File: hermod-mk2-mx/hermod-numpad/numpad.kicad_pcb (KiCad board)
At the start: 2 copper layers, 92.1 x 99.3 mm, 48 parts

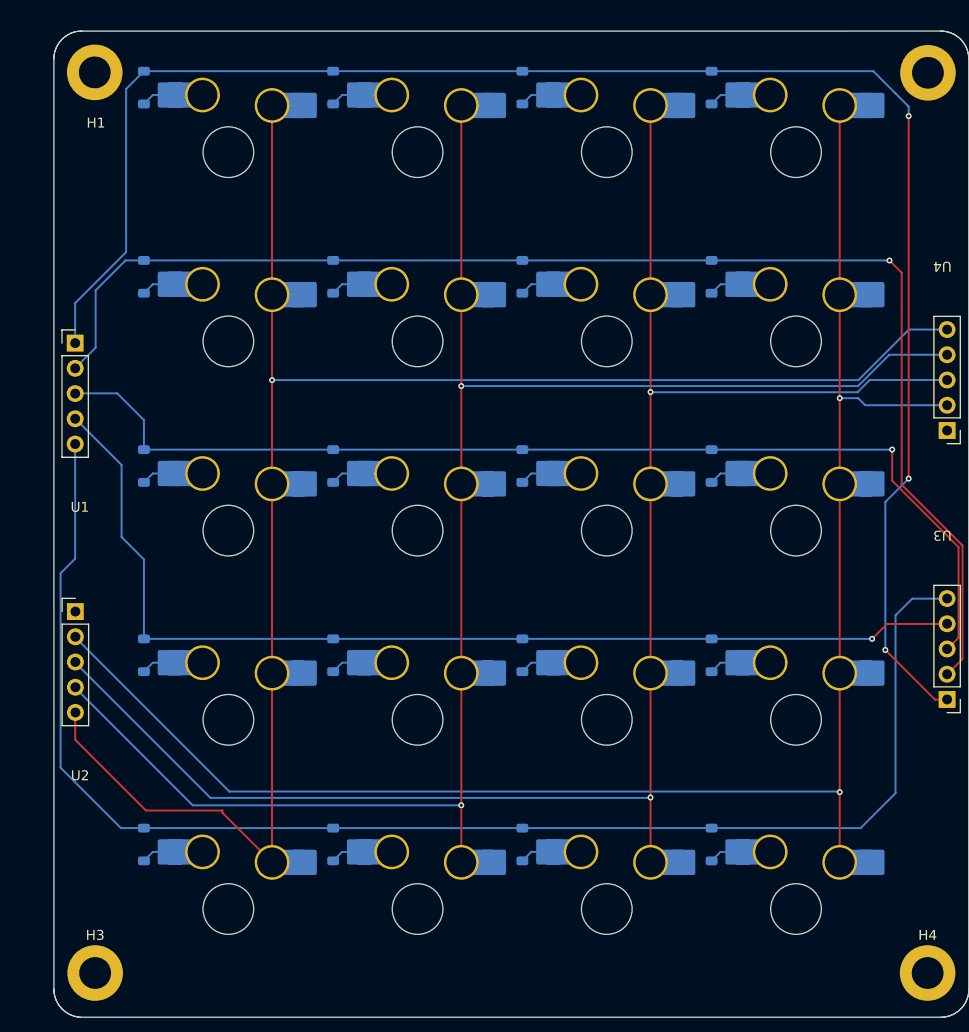
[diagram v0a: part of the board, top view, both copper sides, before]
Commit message: UPdated Hermod Mk 2 to have ks33 and choc v2 footprints
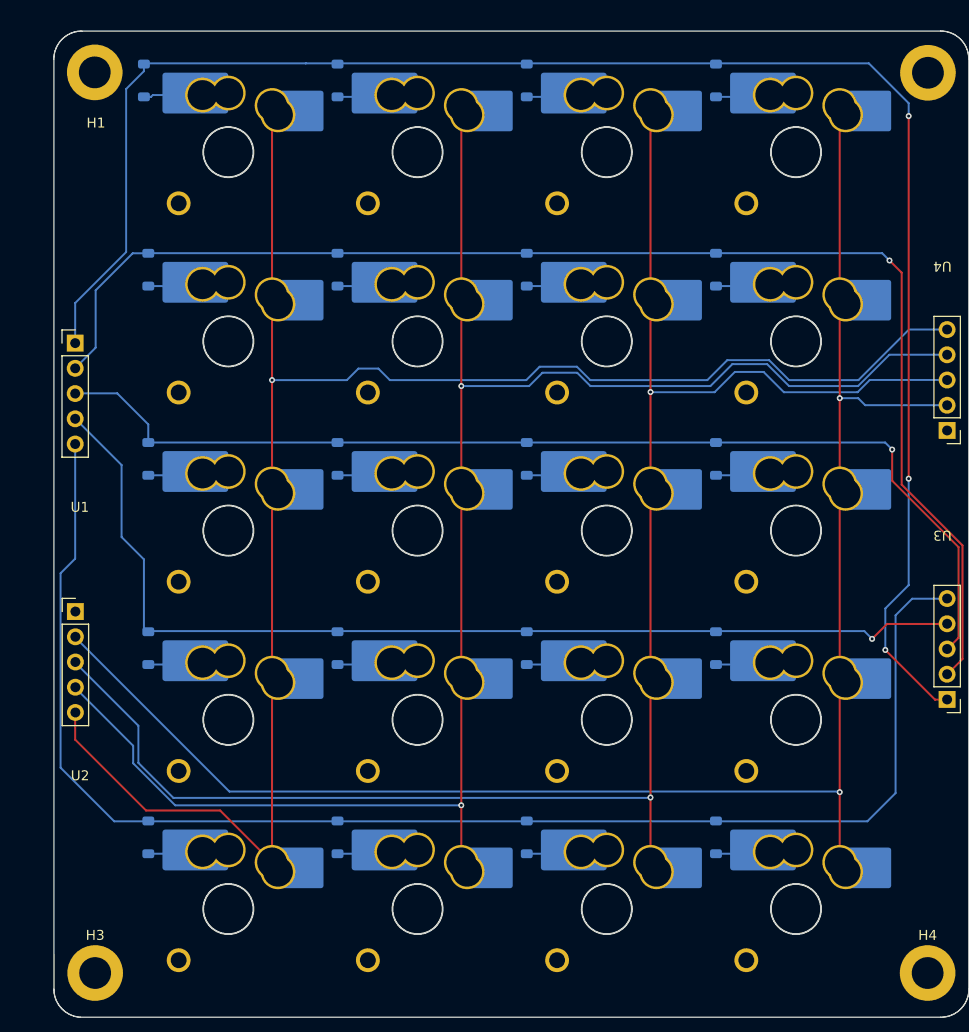
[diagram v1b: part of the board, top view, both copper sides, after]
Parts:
- CH1, CH10, CH11, CH12, CH13, CH14, CH15, CH16, CH17, CH18, CH19, CH2, CH20, CH3, CH4, CH5, CH6, CH7, CH8, CH9: footprint Gateron_KS33_Hotswap:Gateron-KS33-Hotswap-1U -> ModHob:KS33_Choc-v2_HS_1U
- moved D10 0.84 mm to (49.1, 69.0)
- moved D14 0.84 mm to (49.1, 88.0)
- moved D18 0.84 mm to (49.1, 107.1)
- moved D2 0.84 mm to (49.1, 30.9)
- moved D6 0.84 mm to (49.1, 49.9)
- moved D11 0.84 mm to (68.1, 69.0)
- moved D12 0.84 mm to (87.2, 69.0)
- moved D13 0.84 mm to (30.0, 88.0)
- moved D15 0.84 mm to (68.1, 88.0)
- moved D16 0.84 mm to (87.2, 88.0)
- moved D17 0.84 mm to (30.0, 107.1)
- moved D19 0.84 mm to (68.1, 107.1)
- moved D20 0.84 mm to (87.2, 107.1)
- moved D3 0.84 mm to (68.1, 30.9)
- moved D4 0.84 mm to (87.2, 30.9)
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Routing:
- net col8: track 170.2 -> 174.2 mm
- net col9: track 170.2 -> 174.0 mm
- net col7: track 174.0 -> 177.6 mm
- net Net-(D13-A): track 3.04 -> 5.98 mm
- net Net-(D8-A): track 3.04 -> 5.33 mm
- net Net-(D12-A): track 3.04 -> 5.33 mm
- net Net-(D16-A): track 3.04 -> 5.33 mm
- net Net-(D9-A): track 3.04 -> 5.33 mm
- net Net-(D7-A): track 3.04 -> 5.33 mm
- net Net-(D14-A): track 3.04 -> 5.33 mm
- net Net-(D11-A): track 3.04 -> 5.33 mm
- net Net-(D10-A): track 3.04 -> 5.33 mm
- net Net-(D15-A): track 3.04 -> 5.33 mm
- net Net-(D6-A): track 3.04 -> 5.33 mm
- net Net-(D5-A): track 3.04 -> 5.33 mm
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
